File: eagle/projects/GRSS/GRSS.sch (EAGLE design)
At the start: 33 parts, among them J1 MOL-SL-2-RA, J10 MOL-SL-2-RA, J11 M02PTH, J2 MOL-SL-2-RA, J3 MOL-SL-2-RA, J4 MOL-SL-2-RA, J5 MOL-SL-2-RA, J6 MOL-SL-2-RA, J7 MOL-SL-2-RA, J8 MOL-SL-2-RA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

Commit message: A few 0805 caps added to lib and now GRSS jelly bean all 0805 (just did caps)
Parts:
- C1: device grss:CAP_100NF0_0603 -> grss:CAP_100NF0_0805
- C2: device grss:CAP_10UF0_0603 -> grss:CAP_10UF0_0805
- C3: device grss:CAP_2UF2_0603 -> grss:CAP_2UF2_0805
- C4: device grss:CAP_1UF0_0603 -> grss:CAP_1UF0_0805
- C5: device grss:CAP_10PF0_0603 -> grss:CAP_10PF0_0805
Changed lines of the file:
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@@
 <part name="R3" library="grss" deviceset="RES" device="_0805" technology="_100R0" value="100"/>
 <part name="R4" library="grss" deviceset="RES" device="_0805" technology="_240R0" value="240k"/>
-<part name="C1" library="grss" deviceset="CAP" device="_0603" technology="_100NF0" value="100nF"/>
-<part name="C2" library="grss" deviceset="CAP" device="_0603" technology="_10UF0" value="10uF"/>
-<part name="C3" library="grss" deviceset="CAP" device="_0603" technology="_2UF2" value="2.2uF"/>
-<part name="C4" library="grss" deviceset="CAP" device="_0603" technology="_1UF0" value="1uF"/>
-<part name="C5" library="grss" deviceset="CAP" device="_0603" technology="_10PF0" value="10pF"/>
+<part name="C1" library="grss" deviceset="CAP" device="_0805" technology="_100NF0" value="100nF"/>
+<part name="C2" library="grss" deviceset="CAP" device="_0805" technology="_10UF0" value="10uF"/>
+<part name="C3" library="grss" deviceset="CAP" device="_0805" technology="_2UF2" value="2.2uF"/>
+<part name="C4" library="grss" deviceset="CAP" device="_0805" technology="_1UF0" value="1uF"/>
+<part name="C5" library="grss" deviceset="CAP" device="_0805" technology="_10PF0" value="10pF"/>
 <part name="J11" library="grss" deviceset="M02" device="PTH" value="M02PTH"/>
 <part name="FRAME1" library="frames" deviceset="A4L-LOC" device=""/>

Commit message: battery holder pn update
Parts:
- BATT: device grss:BC9VPC -> grss:BH9VPC
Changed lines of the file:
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@@
 </classes>
 <parts>
-<part name="BATT" library="grss" deviceset="BC9VPC" device="" value="9V"/>
+<part name="BATT" library="grss" deviceset="BH9VPC" device="" value="9V"/>
 <part name="R1" library="grss" deviceset="RES" device="_0805" technology="_100R0" value="100"/>
 <part name="R2" library="grss" deviceset="RES" device="_0805" technology="_100R0" value="100"/>

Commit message: TP on GND
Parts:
- added TP4: (no value), grss:TEST_POINT_TP10R_SMD_10R_SMD
- C1: value 100nF -> 0.1uF
- C5: value 10pF -> 0.01uF; device grss:CAP_10PF0_0805 -> grss:CAP_10NF0_0805
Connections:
- net GND: now also TP4.TP
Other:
- moved on the sheet: C5
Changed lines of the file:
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@@
 <part name="R3" library="grss" deviceset="RES" device="_0805" technology="_100R0" value="100"/>
 <part name="R4" library="grss" deviceset="RES" device="_0805" technology="_240R0" value="240k"/>
-<part name="C1" library="grss" deviceset="CAP" device="_0805" technology="_100NF0" value="100nF"/>
+<part name="C1" library="grss" deviceset="CAP" device="_0805" technology="_100NF0" value="0.1uF"/>
 <part name="C2" library="grss" deviceset="CAP" device="_0805" technology="_10UF0" value="10uF"/>
 <part name="C3" library="grss" deviceset="CAP" device="_0805" technology="_2UF2" value="2.2uF"/>
 <part name="C4" library="grss" deviceset="CAP" device="_0805" technology="_1UF0" value="1uF"/>
-<part name="C5" library="grss" deviceset="CAP" device="_0805" technology="_10PF0" value="10pF"/>
+<part name="C5" library="grss" deviceset="CAP" device="_0805" technology="_10NF0" value="0.01uF"/>
 <part name="J11" library="grss" deviceset="M02" device="PTH" value="M02PTH"/>
 <part name="FRAME1" library="frames" deviceset="A4L-LOC" device=""/>
@@
 <part name="U$2" library="grss" deviceset="BLOCK_DIAGRAM" device=""/>
 <part name="R5" library="grss" deviceset="RES" device="_0805" technology="_47R0" value="4.7k"/>
+<part name="TP4" library="grss" deviceset="TEST_POINT" device="_10R_SMD" technology="_TP10R_SMD"/>
 </parts>
 <sheets>
@@
 <instance part="C3" gate="G$1" x="-53.34" y="101.6"/>
 <instance part="C4" gate="G$1" x="-170.18" y="165.1"/>
-<instance part="C5" gate="G$1" x="-60.96" y="101.6"/>
+<instance part="C5" gate="G$1" x="-63.5" y="101.6"/>
 <instance part="J11" gate="G$1" x="-185.42" y="154.94"/>
 <instance part="FRAME1" gate="G$1" x="-195.58" y="48.26"/>
@@
 <instance part="H4" gate="G$1" x="-116.84" y="66.04"/>
 <instance part="R5" gate="G$1" x="-37.846" y="97.79" rot="R90"/>
+<instance part="TP4" gate="G$1" x="-111.76" y="96.52"/>
 </instances>
 <busses>
@@
 <segment>
 <pinref part="C5" gate="G$1" pin="1"/>
-<wire x1="-93.98" y1="170.18" x2="-60.96" y2="170.18" width="0.1524" layer="91"/>
-<wire x1="-60.96" y1="170.18" x2="-60.96" y2="106.68" width="0.1524" layer="91"/>
+<wire x1="-93.98" y1="170.18" x2="-63.5" y2="170.18" width="0.1524" layer="91"/>
+<wire x1="-63.5" y1="170.18" x2="-63.5" y2="106.68" width="0.1524" layer="91"/>
 <pinref part="U3" gate="A" pin="BP"/>
-<label x="-60.452" y="170.18" size="1.778" layer="95"/>
+<label x="-62.992" y="170.18" size="1.778" layer="95"/>
 </segment>
 </net>
@@
 <segment>
 <pinref part="BATT" gate="G$1" pin="V-"/>
-<wire x1="-53.34" y1="91.44" x2="-60.96" y2="91.44" width="0.1524" layer="91"/>
-<wire x1="-60.96" y1="91.44" x2="-149.86" y2="91.44" width="0.1524" layer="91"/>
+<wire x1="-53.34" y1="91.44" x2="-63.5" y2="91.44" width="0.1524" layer="91"/>
+<wire x1="-63.5" y1="91.44" x2="-111.76" y2="91.44" width="0.1524" layer="91"/>
+<wire x1="-111.76" y1="91.44" x2="-149.86" y2="91.44" width="0.1524" layer="91"/>
 <wire x1="-149.86" y1="91.44" x2="-160.02" y2="91.44" width="0.1524" layer="91"/>
 <wire x1="-160.02" y1="91.44" x2="-170.18" y2="91.44" width="0.1524" layer="91"/>
@@
 <wire x1="-170.18" y1="154.94" x2="-170.18" y2="134.62" width="0.1524" layer="91"/>
 <pinref part="C5" gate="G$1" pin="2"/>
-<wire x1="-60.96" y1="99.06" x2="-60.96" y2="91.44" width="0.1524" layer="91"/>
+<wire x1="-63.5" y1="99.06" x2="-63.5" y2="91.44" width="0.1524" layer="91"/>
 <pinref part="C3" gate="G$1" pin="2"/>
 <wire x1="-53.34" y1="99.06" x2="-53.34" y2="91.44" width="0.1524" layer="91"/>
 <junction x="-170.18" y="134.62"/>
-<junction x="-60.96" y="91.44"/>
+<junction x="-63.5" y="91.44"/>
 <junction x="-149.86" y="91.44"/>
 <junction x="-160.02" y="91.44"/>
@@
 <wire x1="-37.846" y1="91.44" x2="-37.846" y2="92.71" width="0.1524" layer="91"/>
 <junction x="-37.846" y="91.44"/>
-</segment>
-</net>
+<pinref part="TP4" gate="G$1" pin="TP"/>
+<junction x="-111.76" y="91.44"/>
+</segment>
+</net>

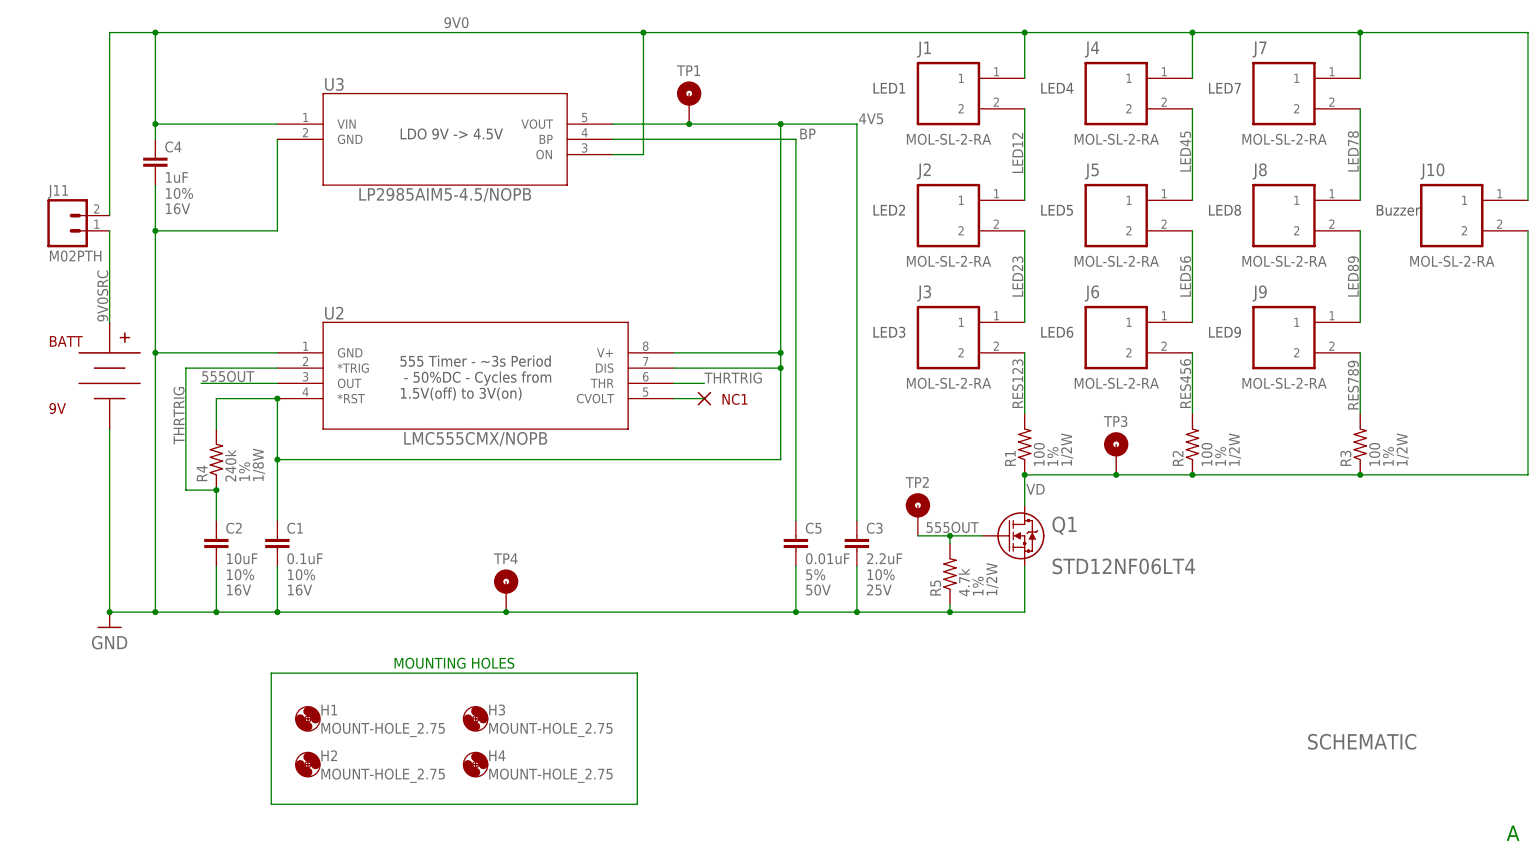
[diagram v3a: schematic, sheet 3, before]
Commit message: Added 3.3,4.7uF,1k to lib, Schematic now at RevB, Battery flipped to bottom of board
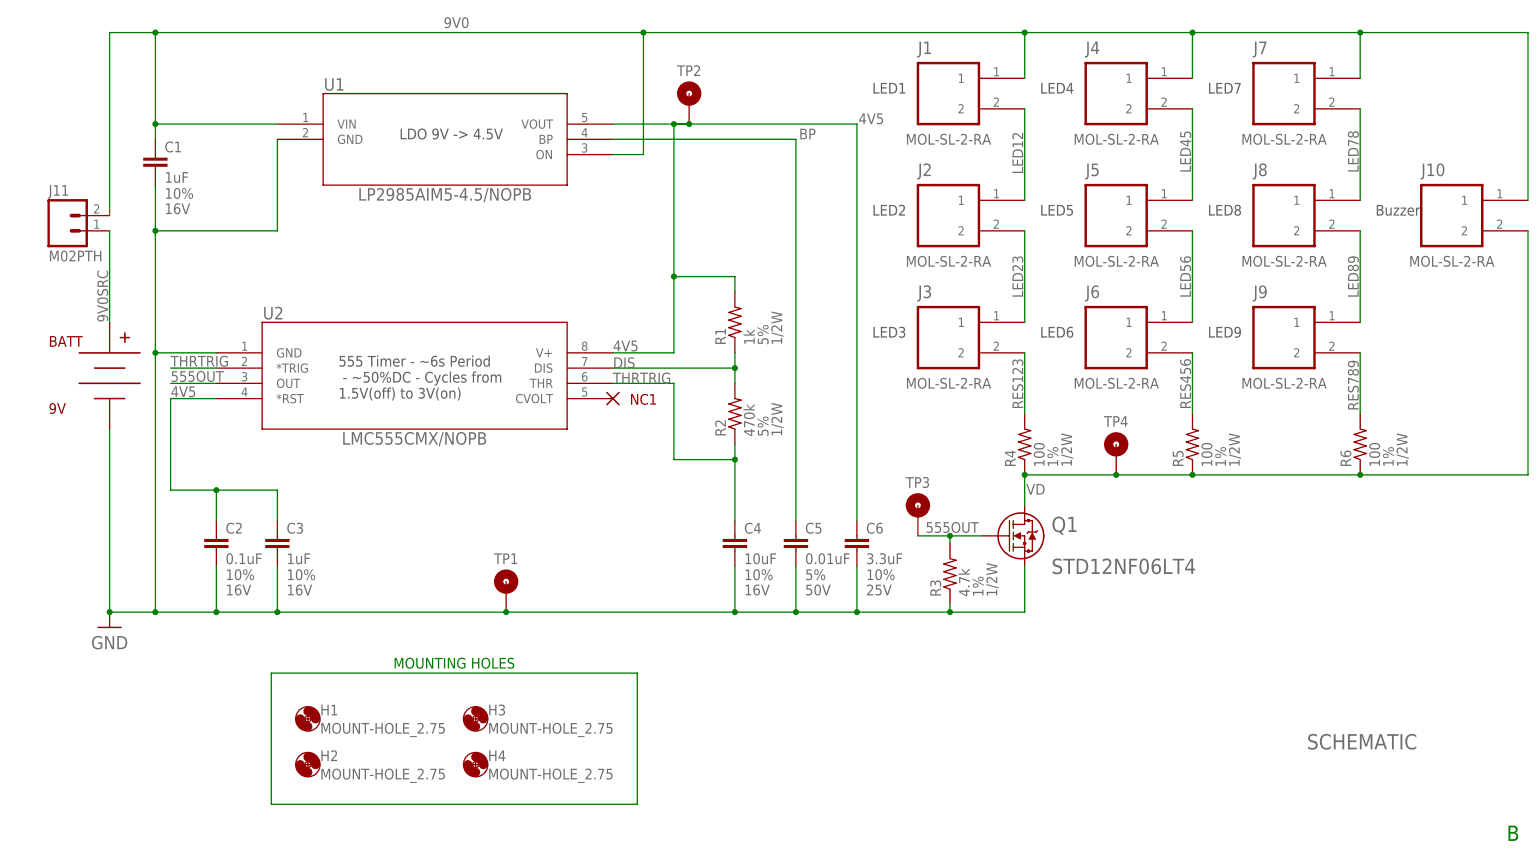
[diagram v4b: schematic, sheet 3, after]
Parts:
- added C6: 3.3uF, grss:CAP_3UF3_0805
- added R6: 100, grss:RES_100R0_0805
- C1: value 0.1uF -> 1uF; device grss:CAP_100NF0_0805 -> grss:CAP_1UF0_0805
- C2: value 10uF -> 0.1uF; device grss:CAP_10UF0_0805 -> grss:CAP_100NF0_0805
- C3: value 2.2uF -> 1uF; device grss:CAP_2UF2_0805 -> grss:CAP_1UF0_0805
- C4: value 1uF -> 10uF; device grss:CAP_1UF0_0805 -> grss:CAP_10UF0_0805
- R1: value 100 -> 1k; device grss:RES_100R0_0805 -> grss:RES_1K0_0805
- R2: value 100 -> 470k; device grss:RES_100R0_0805 -> grss:RES_470K0_0805
- R3: value 100 -> 4.7k; device grss:RES_100R0_0805 -> grss:RES_47R0_0805
- R4: value 240k -> 100; device grss:RES_240R0_0805 -> grss:RES_100R0_0805
- R5: value 4.7k -> 100; device grss:RES_47R0_0805 -> grss:RES_100R0_0805
- TP1: value (none) -> GND
- TP2: value (none) -> 4V5
- TP3: value (none) -> 555OUT
- TP4: value (none) -> VD
- renumbered U3 to U1
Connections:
- new net DIS: R1.1, R2.2, U2.DIS
- net 4V5: now also C2.1, C6.1, R1.2, TP2.TP; no longer C1.1, R4.2, TP1.TP, U2.DIS
- net 555OUT: now also R3.2, TP3.TP; no longer R5.2, TP2.TP
- net 9V0: now also C1.1; no longer C4.1
- net GND: now also C6.2, R3.1, TP1.TP; no longer R5.1, TP4.TP
- net RES123: now also R4.2; no longer R1.2
- net RES456: now also R5.2; no longer R2.2
- net RES789: now also R6.2; no longer R3.2
- net THRTRIG: now also C4.1, R2.1; no longer C2.1, R4.1
- net VD: now also R4.1, R5.1, R6.1, TP4.TP; no longer R1.1, R2.1, R3.1, TP3.TP
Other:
- note added: "555 Timer - ~6s Period - ~50%DC - Cycles from 1.5V(off) to 3V(on)"
- note added: "B"
- note removed: "555 Timer - ~3s Period - 50%DC - Cycles from 1.5V(off) to 3V(on)"
- note removed: "A"
- moved on the sheet: C1, C3, C4, NC1, R1, R2, R3, R4, R5, TP1, TP2, TP3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

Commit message: rough initial placement... 66x50mm
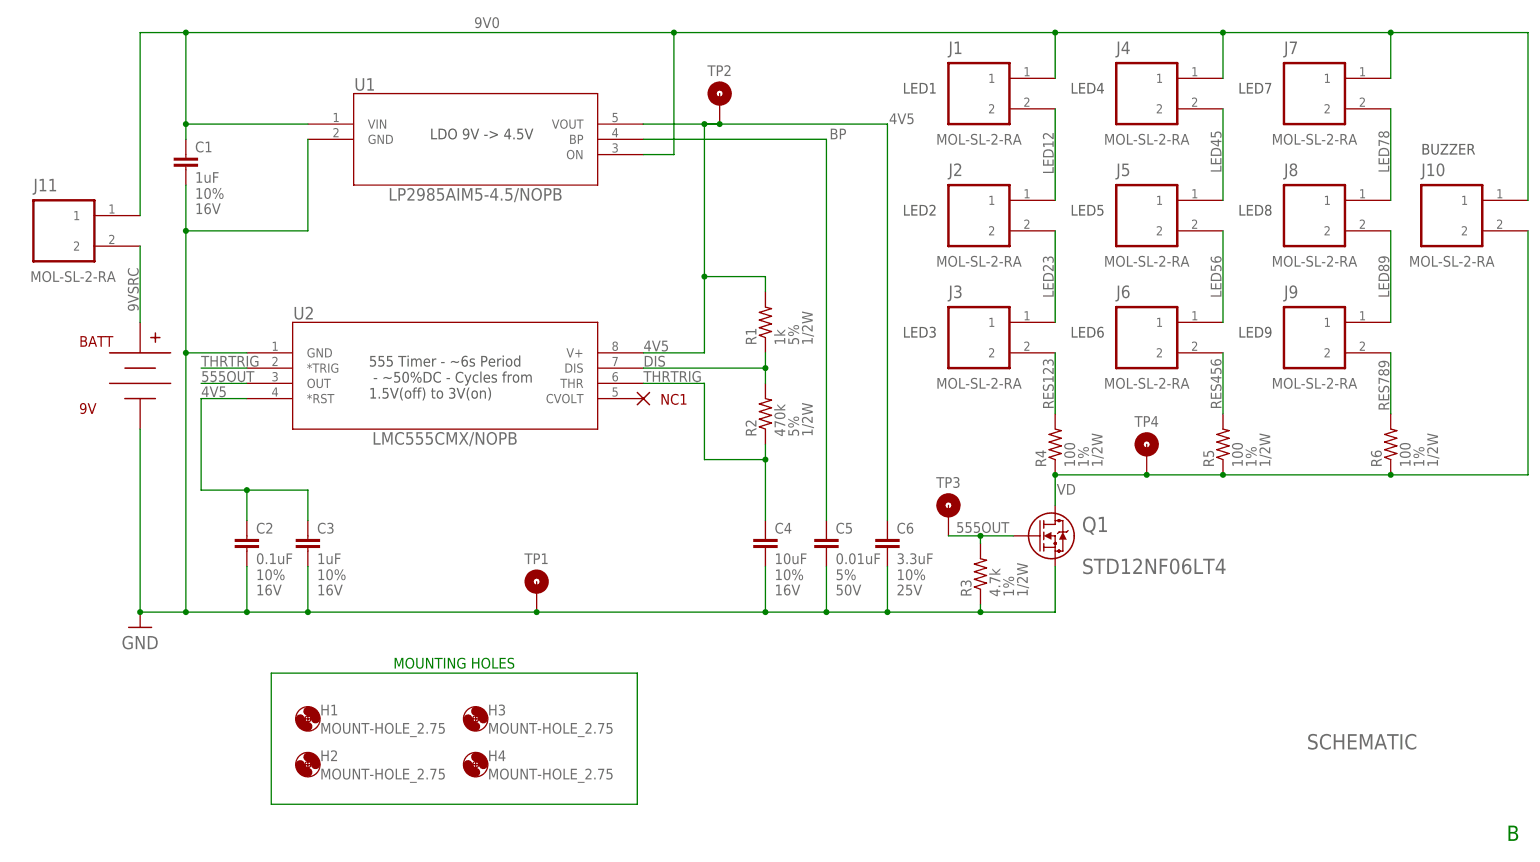
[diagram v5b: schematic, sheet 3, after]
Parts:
- J11: value M02PTH -> MOL-SL-2-RA; device grss:M02PTH -> grss:MOLSL_2PIN_SL2RA_RA
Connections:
- removed net 9V0SRC: BATT.V+, J11.1
- new net 9VSRC: BATT.V+, J11.2
- net 9V0: now also J11.1; no longer J11.2
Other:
- note added: "BUZZER"
- note removed: "Buzzer"
- moved on the sheet: BATT, C1, C2, C3, C4, C5, C6, J1, J11, J2, J3, J4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

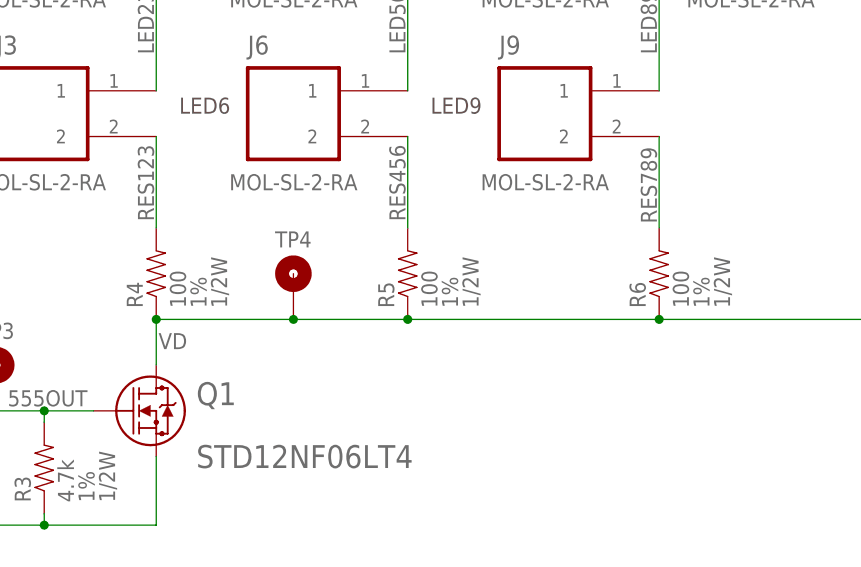
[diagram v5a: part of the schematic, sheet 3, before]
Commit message: Updated LED series resistor to 200 ohms
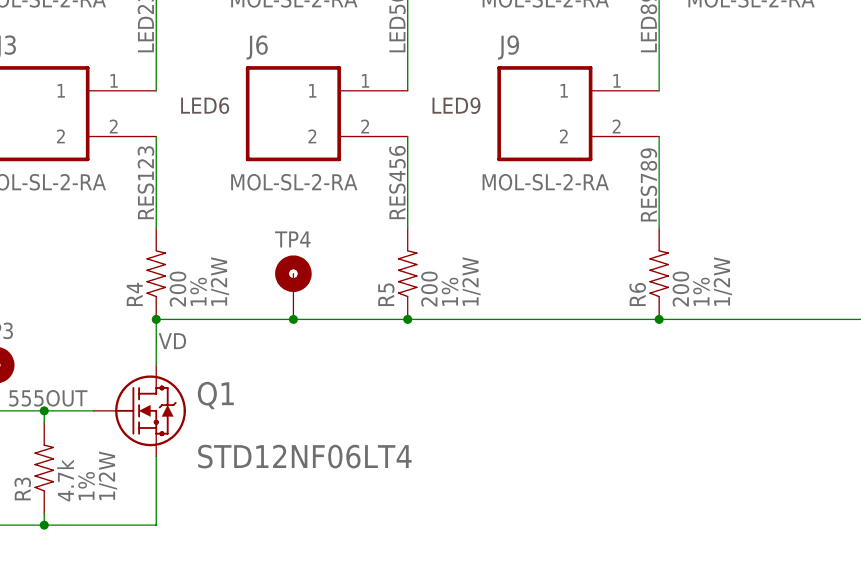
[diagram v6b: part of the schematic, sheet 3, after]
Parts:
- R4, R5, R6: value 100 -> 200; device grss:RES_100R0_0805 -> grss:RES_200R0_0805
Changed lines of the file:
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@@
 <parts>
 <part name="BATT" library="grss" deviceset="BH9VPC" device="" value="9V"/>
-<part name="R4" library="grss" deviceset="RES" device="_0805" technology="_100R0" value="100"/>
-<part name="R5" library="grss" deviceset="RES" device="_0805" technology="_100R0" value="100"/>
-<part name="R6" library="grss" deviceset="RES" device="_0805" technology="_100R0" value="100"/>
+<part name="R4" library="grss" deviceset="RES" device="_0805" technology="_200R0" value="200"/>
+<part name="R5" library="grss" deviceset="RES" device="_0805" technology="_200R0" value="200"/>
+<part name="R6" library="grss" deviceset="RES" device="_0805" technology="_200R0" value="200"/>
 <part name="R2" library="grss" deviceset="RES" device="_0805" technology="_470K0" value="470k"/>
 <part name="C2" library="grss" deviceset="CAP" device="_0805" technology="_100NF0" value="0.1uF"/>
